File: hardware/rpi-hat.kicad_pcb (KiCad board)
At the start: 2 copper layers, 65 x 56 mm, 86 parts, among them J1 Conn_02x20_Odd_Even__Rpi, J10 A1, J11 A3, J12 A4, J13 A5, J14 A6, J15 Conn_01x01_Male, J16 Conn_01x02_Male, J17 Fan 1, J18 Fan 2, J2 USART, J3 I2C 3.3V, J4 I2C 3.3V, J5 I2C 5V, J6 PPS, J7 10103594-0001LF, J8 Jumper, J9 A0, U1 Fan Driver, U10 Vreg, U11 V Shift, U2 EEPROM, U3 Buffer, U4 BSS138, U5 BSS138, U6 Buffer, U7 DAC, U8 Multiplexer, U9 ADC

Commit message: Update PCB
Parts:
- removed J18: Fan 2, zephyrus-iaq:SM02B-SRSS-TB(LF)(SN)
- removed R18: 3.3k, Resistor_SMD:R_0805_2012Metric
- added J16: I2C 5V, zephyrus-iaq:JST_SM04B-SRSS-TB(LF)(SN), F.Cu at (260.0, 137.7)
- added R17: 3.3k, Resistor_SMD:R_0805_2012Metric, F.Cu at (212.9, 123.0)
- J11: value A3 -> A2
- J12: value A4 -> A3
- J13: value A5 -> A4
- J14: value A6 -> A5
- J15: value Conn_01x01_Male -> Alert
- J17: value Fan 1 -> PPS; footprint zephyrus-iaq:SM02B-SRSS-TB(LF)(SN) -> Connector_PinSocket_2.54mm:PinSocket_1x01_P2.54mm_Vertical
- J3: value I2C 3.3V -> Jumper; footprint zephyrus-iaq:JST_SM04B-SRSS-TB(LF)(SN) -> Connector_PinSocket_2.54mm:PinSocket_1x02_P2.54mm_Vertical
- J4: value I2C 3.3V -> Fan 1; footprint zephyrus-iaq:JST_SM04B-SRSS-TB(LF)(SN) -> zephyrus-iaq:SM02B-SRSS-TB(LF)(SN)
- J5: value I2C 5V -> Fan 2; footprint SM04B-SRSS-TB_LF__SN_:JST_SM04B-SRSS-TB(LF)(SN) -> zephyrus-iaq:SM02B-SRSS-TB(LF)(SN)
- J6: value PPS -> I2C 3.3V; footprint Connector_PinSocket_2.54mm:PinSocket_1x01_P2.54mm_Vertical -> zephyrus-iaq:JST_SM04B-SRSS-TB(LF)(SN)
- J8: value Jumper -> I2C 3.3V; footprint Connector_PinSocket_2.54mm:PinSocket_1x02_P2.54mm_Vertical -> zephyrus-iaq:JST_SM04B-SRSS-TB(LF)(SN)
- R1: value 3.9k -> 1k
- R16: value 1.8k -> 3.3k
- R2: value 3.9k -> DNP
- R24: value 1k -> 287
- R5: value 1k -> 3.9k
- R6: value 330 -> 3.9k; footprint Resistor_SMD:R_0805_2012Metric -> Resistor_SMD:R_0805_2012Metric_Pad1.15x1.40mm_HandSolder
- R8: value DNP -> 330; footprint Resistor_SMD:R_0805_2012Metric_Pad1.15x1.40mm_HandSolder -> Resistor_SMD:R_0805_2012Metric
- U1: value Fan Driver -> EEPROM; footprint zephyrus-iaq:SON50P200X200X80-9N -> zephyrus-iaq:SOIC127P600X175-8N
- U10: value Vreg -> 5V
- U11: value V Shift -> 3.3V -> 5V
- U2: value EEPROM -> FAN; footprint CAT24C32WI-GT3:SOIC127P600X175-8N -> zephyrus-iaq:SON50P200X200X80-9N
- U3, U6: value Buffer -> BUF
- U8: value Multiplexer -> MUX to ADC
- moved MK4 75.7 mm to (203.6, 97.7)
- moved MK2 57.9 mm to (261.5, 146.5)
- moved MK1 48.8 mm to (203.6, 146.5)
- moved J5 22.9 mm to (262.0, 114.8)
- moved J4 20.4 mm to (262.1, 109.2)
- moved J8 19.1 mm to (260.0, 121.5), turned to 90 degrees
- moved J3 19.0 mm to (262.5, 102.6), turned to 0 degrees
- moved U1 17.7 mm to (244.5, 104.2)
- moved U2 17.7 mm to (248.4, 121.4)
- moved J17 14.1 mm to (255.5, 121.7), turned to 0 degrees
- moved R8 12.3 mm to (254.0, 115.9), turned to 270 degrees
- moved J6 8.82 mm to (260.0, 129.5), turned to 90 degrees
- moved R7 7.16 mm to (254.1, 108.7)
- moved R2 6.07 mm to (259.1, 103.4), turned to 90 degrees
- moved R6 5.29 mm to (253.0, 103.5)
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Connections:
- D2 pad 2: /FAN_OUT1 -> /Fan_Control/FAN_OUT1
- D3 pad 2: /FAN_OUT2 -> /Fan_Control/FAN_OUT2
- J17 pad 1: /FAN_OUT1 -> /GPIO18(GEN1)(PWM0)
- J3 pad 1: GND -> Net-(J3-Pad1)
- J3 pad 2: +3V3 -> GND
- J4 pad 1: GND -> /Fan_Control/FAN_OUT1
- J4 pad 2: +3V3 -> GND
- J4 pad 3: /GPIO3(SCL1) -> (no net)
- J4 pad 4: /GPIO2(SDA1) -> (no net)
- J5 pad 1: GND -> /Fan_Control/FAN_OUT2
- J5 pad 2: +5V -> GND
- J5 pad 3: /SDA_5 -> (no net)
- J5 pad 4: /SCL_5 -> (no net)
- J6 pad 1: /GPIO18(GEN1)(PWM0) -> GND
- J8 pad 1: Net-(J8-Pad1) -> GND
- J8 pad 2: GND -> +3V3
- R1 pad 2: /ID_SD_EEPROM -> Net-(J3-Pad1)
- R2 pad 1: +3V3 -> GND
- R2 pad 2: /ID_SC_EEPROM -> Net-(J3-Pad1)
- R5 pad 2: Net-(J8-Pad1) -> /ID_SD_EEPROM
- R6 pad 1: Net-(D2-Pad1) -> +3V3
- R6 pad 2: GND -> /ID_SC_EEPROM
- R7 pad 1: Net-(D3-Pad1) -> Net-(D2-Pad1)
- R8 pad 1: GND -> Net-(D3-Pad1)
- R8 pad 2: Net-(J8-Pad1) -> GND
- U1 pad 1: +5V -> GND
- U1 pad 2: /FAN_OUT1 -> GND
- U1 pad 3: /FAN_OUT2 -> GND
- U1 pad 5: /FAN_PWM1 -> /ID_SD_EEPROM
- U1 pad 6: /FAN_PWM0 -> /ID_SC_EEPROM
- U1 pad 7: /FAN_nSLEEP -> Net-(J3-Pad1)
- U11 pad 11: /ADC_Subsystem/MUL_INH_5V -> Net-(U11-Pad11)
- U11 pad 12: GND -> Net-(U11-Pad12)
- U11 pad 13: /GPIO24(GEN5) -> Net-(U11-Pad13)
- U2 pad 1: GND -> +5V
- U2 pad 2: GND -> /Fan_Control/FAN_OUT1
- U2 pad 3: GND -> /Fan_Control/FAN_OUT2
- U2 pad 5: /ID_SD_EEPROM -> /FAN_PWM1
- U2 pad 6: /ID_SC_EEPROM -> /FAN_PWM0
- U2 pad 7: Net-(J8-Pad1) -> /FAN_nSLEEP
- U8 pad 6: /ADC_Subsystem/MUL_INH_5V -> GND
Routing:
- net /ADC_Subsystem/MUL_INH_5V: track 61.7 -> 0.00 mm, vias 2 -> 0
- net GND: track 214.8 -> 251.9 mm, vias 46 -> 48
- net /GPIO24(GEN5): track 98.3 -> 71.9 mm, vias 4 -> 2
- net /Fan_Control/FAN_OUT1: track 0.00 -> 20.7 mm
- net /FAN_OUT1: track 20.7 -> 0.00 mm
- net Net-(J3-Pad1): track 0.00 -> 19.0 mm
- net Net-(J8-Pad1): track 18.8 -> 0.00 mm
- net /Fan_Control/FAN_OUT2: track 0.00 -> 17.8 mm
- net /FAN_OUT2: track 17.7 -> 0.00 mm
- net /GPIO2(SDA1): track 102.9 -> 107.4 mm
- net /GPIO3(SCL1): track 119.6 -> 115.6 mm
- net +3V3: track 181.1 -> 180.9 mm, vias 10 -> 11
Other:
- board text added: "Rev. A 10/2019"
- board text added: "to BUF"

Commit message: Update PCB
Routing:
- net GND: track 251.9 -> 212.1 mm, vias 48 -> 44
- net /SCL_5: track 88.5 -> 87.3 mm

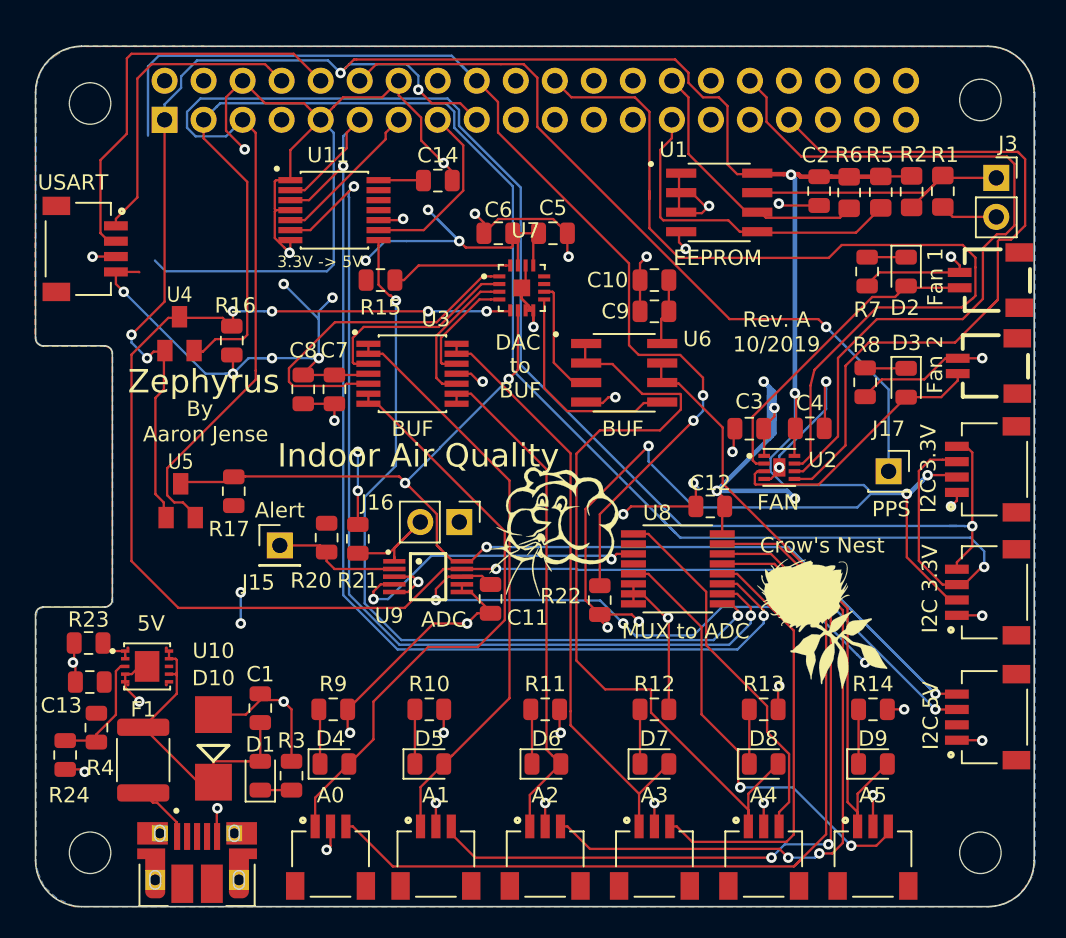
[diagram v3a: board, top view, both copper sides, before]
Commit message: Change Buffer footprint.
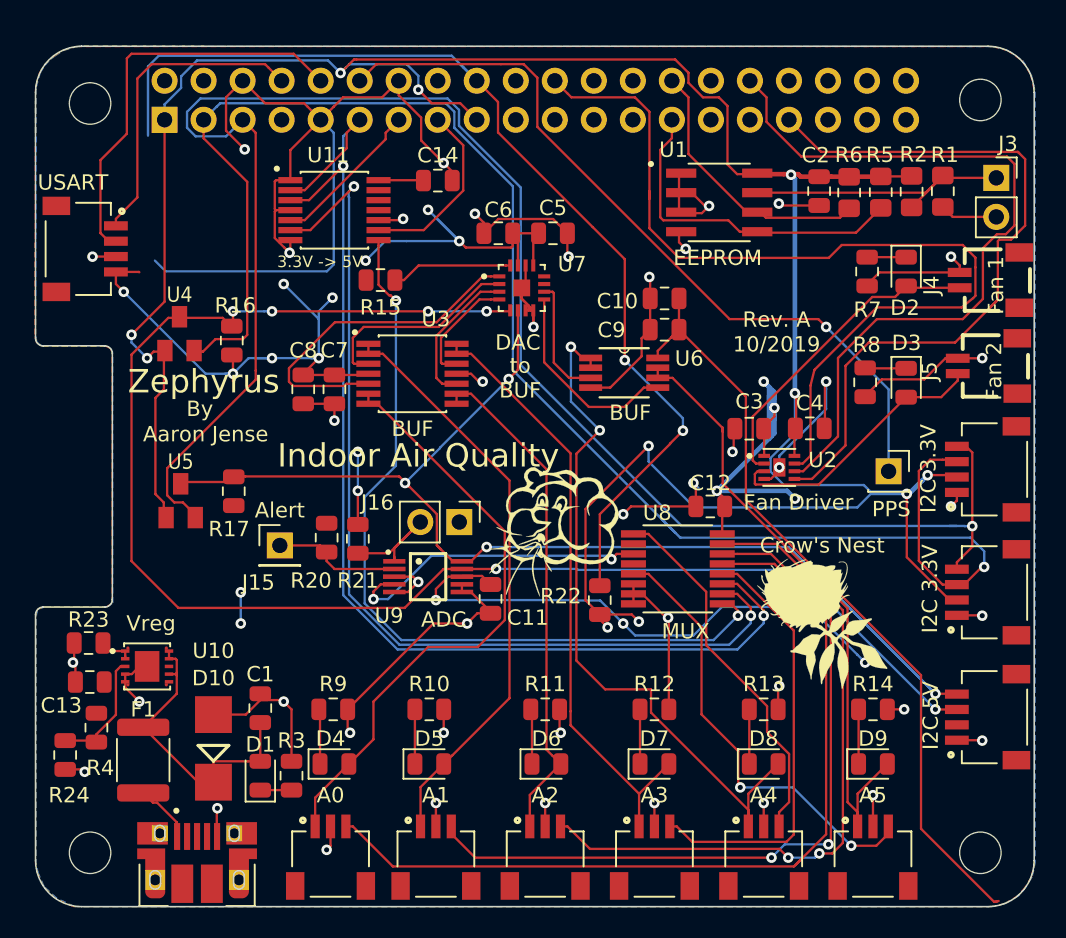
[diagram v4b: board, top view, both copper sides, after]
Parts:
- U10: value 5V -> Vreg
- U2: value FAN -> Fan Driver
- U6: footprint zephyrus-iaq:SOIC127P600X175-8N -> zephyrus-iaq:SOP65P490X110-8N
- U8: value MUX to ADC -> MUX
- moved C9 1.36 mm to (240.9, 112.4)
- moved C10 1.36 mm to (240.9, 110.4)
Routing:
- net +5V: track 139.6 -> 186.4 mm
- net /Analog_Sensors/BUF_OUT_4: track 53.7 -> 47.0 mm, vias 0 -> 2
- net GND: track 212.1 -> 215.9 mm, vias 44 -> 43
- net /GPIO24(GEN5): track 71.9 -> 69.2 mm
- net /Analog_Sensors/DAC_OUT_E: track 14.2 -> 13.2 mm

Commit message: Update silk screen
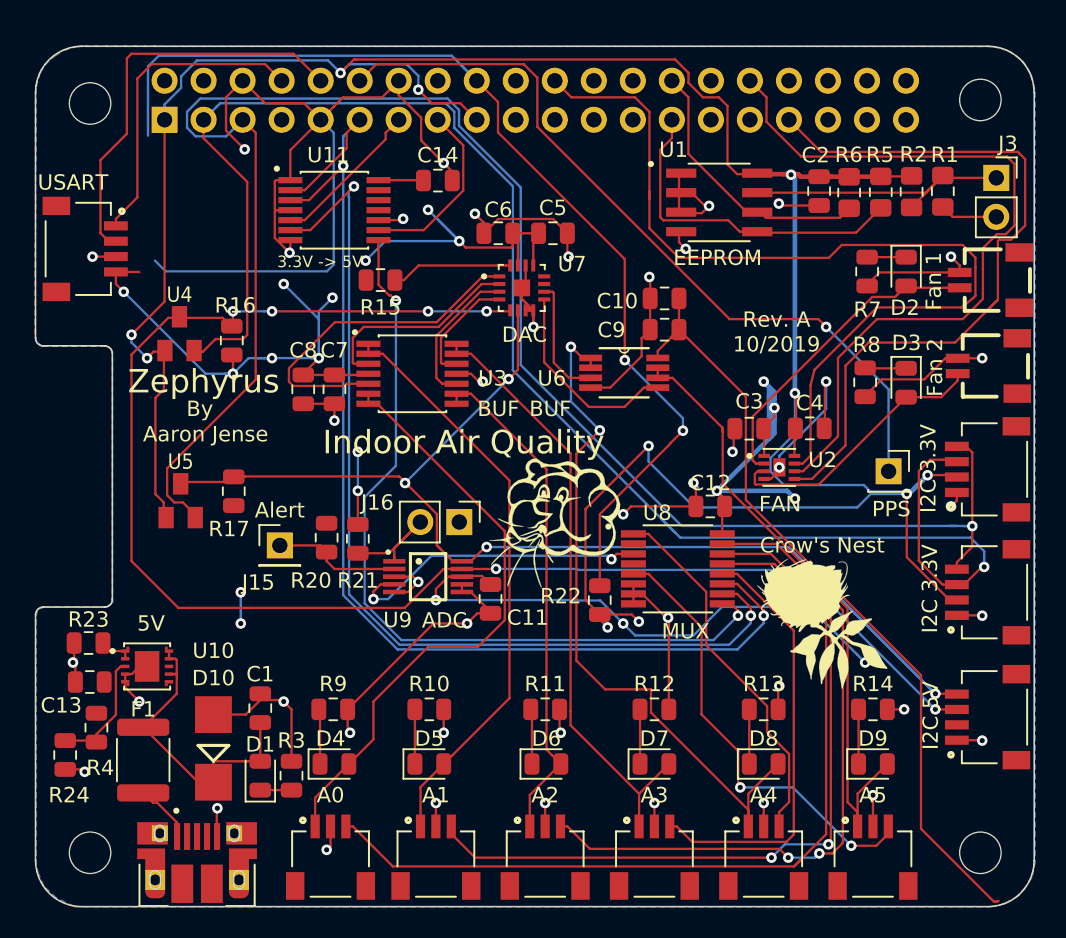
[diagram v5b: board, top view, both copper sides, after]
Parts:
- U10: value Vreg -> 5V
- U2: value Fan Driver -> FAN
- moved G*** 0.57 mm to (233.7, 125.0)
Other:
- board text removed: "to BUF"
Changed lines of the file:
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@@
   (general
     (thickness 1.6)
-    (drawings 53)
+    (drawings 52)
     (tracks 1027)
     (zones 0)
@@
   )
   (layers
-    (0 F.Cu signal)
-    (31 B.Cu signal)
+    (0 F.Cu signal hide)
+    (31 B.Cu signal hide)
     (32 B.Adhes user)
     (33 F.Adhes user)
@@
     (at 238.3155 115.2525)
     (attr smd)
-    (fp_text reference U6 (at 4.2291 -0.9271) (layer F.SilkS)
+    (fp_text reference U6 (at -4.7117 0.3683) (layer F.SilkS)
       (effects (font (size 1 1) (thickness 0.15)))
     )
-    (fp_text value BUF (at 0.3937 2.6035) (layer F.SilkS)
+    (fp_text value BUF (at -4.8133 2.3495) (layer F.SilkS)
       (effects (font (size 1 1) (thickness 0.15)))
     )
@@
     (descr <b>SM02B-SRSS-TB</b><br>)
     (attr smd)
-    (fp_text reference J5 (at -0.346857 -3.81 90) (layer F.SilkS)
+    (fp_text reference J5 (at -0.2286 0.4572 90) (layer F.SilkS) hide
       (effects (font (size 1.00248 1.00248) (thickness 0.05)))
     )
-    (fp_text value "Fan 2" (at -0.347136 0.391283 90) (layer F.SilkS)
-      (effects (font (size 1.00328 1.00328) (thickness 0.05)))
+    (fp_text value "Fan 2" (at -0.1016 -3.4544 90) (layer F.SilkS)
+      (effects (font (size 1.00328 1.00328) (thickness 0.15)))
     )
     (fp_line (start 2 -1.65) (end 1.1 -1.65) (layer F.SilkS) (width 0.254))
@@
     (descr <b>SM02B-SRSS-TB</b><br>)
     (attr smd)
-    (fp_text reference J4 (at -0.346857 -3.81 90) (layer F.SilkS)
+    (fp_text reference J4 (at -0.254 0.3302 90) (layer F.SilkS) hide
       (effects (font (size 1.00248 1.00248) (thickness 0.05)))
     )
-    (fp_text value "Fan 1" (at -0.347136 0.391283 90) (layer F.SilkS)
-      (effects (font (size 1.00328 1.00328) (thickness 0.05)))
+    (fp_text value "Fan 1" (at -0.0762 -3.6576 90) (layer F.SilkS)
+      (effects (font (size 1.00328 1.00328) (thickness 0.15)))
     )
     (fp_line (start 2 -1.65) (end 1.1 -1.65) (layer F.SilkS) (width 0.254))
@@
       (effects (font (size 1 1) (thickness 0.15)))
     )
-    (fp_text value "Fan Driver" (at 1.2446 2.286) (layer F.SilkS)
+    (fp_text value FAN (at 0.0508 2.3876) (layer F.SilkS)
       (effects (font (size 1 1) (thickness 0.15)))
     )
@@
   )
   (module zephyrus-iaq:wind-lineart (layer F.Cu)
-    (at 233.553 125.603)
+    (at 233.6546 125.0442)
     (fp_text reference G*** (at 4.3688 28.9052) (layer F.SilkS) hide
       (effects (font (size 1.524 1.524) (thickness 0.3)))
@@
       (effects (font (size 1 1) (thickness 0.15)))
     )
-    (fp_text value Vreg (at 0.254 -2.794) (layer F.SilkS)
+    (fp_text value 5V (at 0.254 -2.794) (layer F.SilkS)
       (effects (font (size 1 1) (thickness 0.15)))
     )
@@
     (at 224.536 115.316)
     (attr smd)
-    (fp_text reference U3 (at 1.524 -3.556) (layer F.SilkS)
+    (fp_text reference U3 (at 5.207 0.3048) (layer F.SilkS)
       (effects (font (size 1.00101 1.00101) (thickness 0.15)))
     )
-    (fp_text value BUF (at 0 3.5823) (layer F.SilkS)
+    (fp_text value BUF (at 5.588 2.286) (layer F.SilkS)
       (effects (font (size 1.00065 1.00065) (thickness 0.15)))
     )
@@
     (at 225.552 128.524)
     (attr smd)
-    (fp_text reference U9 (at -2.54 2.54) (layer F.SilkS)
+    (fp_text reference U9 (at -1.9812 2.8194) (layer F.SilkS)
       (effects (font (size 1 1) (thickness 0.15)))
     )
-    (fp_text value ADC (at 1.016 2.794) (layer F.SilkS)
+    (fp_text value ADC (at 1.0668 2.8448) (layer F.SilkS)
       (effects (font (size 1 1) (thickness 0.15)))
     )
@@
       (effects (font (size 1 1) (thickness 0.15)))
     )
-    (fp_text value DAC (at -0.254 3.556) (layer F.SilkS)
+    (fp_text value DAC (at 0.1778 3.048) (layer F.SilkS)
       (effects (font (size 1 1) (thickness 0.15)))
     )
@@
     (effects (font (size 1 1) (thickness 0.25)))
   )
-  (gr_text "to\nBUF" (at 231.5464 115.5954) (layer F.SilkS)
-    (effects (font (size 1 1) (thickness 0.15)))
-  )
   (gr_text "Team Members:\nAaron Jense\nAnthony Ciccotosto\nJustin Smith\nBenjamin Seal\n" (at 254.762 116.459) (layer B.SilkS)
     (effects (font (size 1 1) (thickness 0.25) italic) (justify mirror))
@@
     (effects (font (size 1 1) (thickness 0.25)))
   )
-  (gr_text "Indoor Air Quality" (at 224.917 120.65) (layer F.SilkS)
+  (gr_text "Indoor Air Quality" (at 227.8634 119.7864) (layer F.SilkS)
     (effects (font (size 1.524 1.524) (thickness 0.3)))
   )
